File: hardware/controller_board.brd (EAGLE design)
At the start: 86 x 65.5 mm, 249 parts, among them J1 FRSKY-GIMBAL-FRYSKY, J11 USB-MICROA-AMPHENOL-10118192-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, J2 FRSKY-GIMBAL-FRYSKY, J3 USB-MINIB-EDAC-690-005-299-043, J4 AVR_SPI_PRG_6NS, J5 JUMPER-SMT_2_NC_PASTE_NO-SILK, J8 FRSKY-GIMBAL-2X-SERVO, J9 FRSKY-GIMBAL-2X-SERVO, P1 TEST-POINT, P2 TEST-POINT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

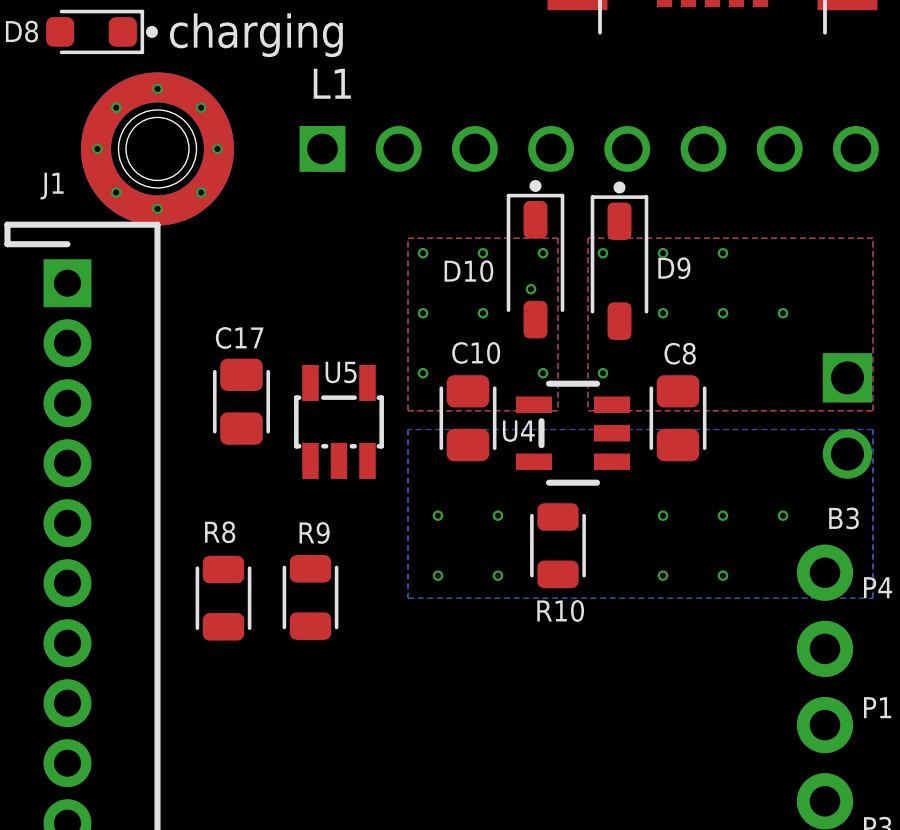
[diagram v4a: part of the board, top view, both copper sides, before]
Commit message: small tweaks to increase symmetry
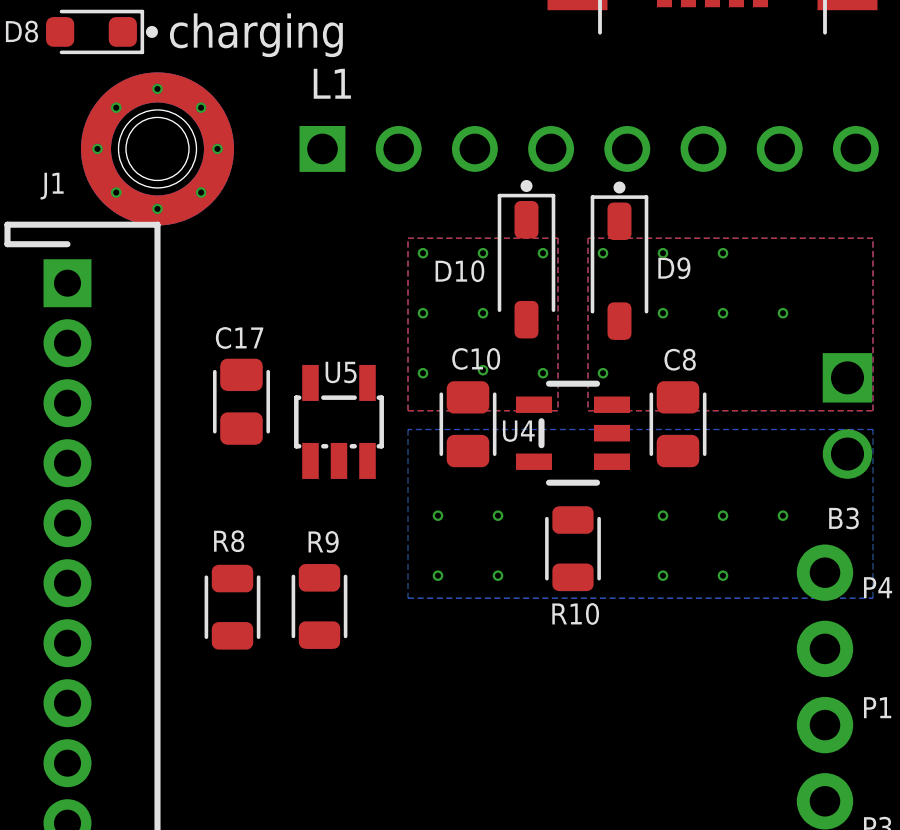
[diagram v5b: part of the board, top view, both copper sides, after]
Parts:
- moved V25 3.14 mm to (-26.6, 10.8)
- moved R10 0.51 mm to (-23.6, 4.80)
- moved R8 0.42 mm to (-35.0, 2.85)
- moved R9 0.42 mm to (-32.1, 2.88)
- moved D10 0.30 mm to (-25.2, 14.1)
- moved C10 0.20 mm to (-27.1, 8.95)
- moved C8 0.20 mm to (-20.1, 8.95)

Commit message: simplify design
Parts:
- R11: value 270 -> 510

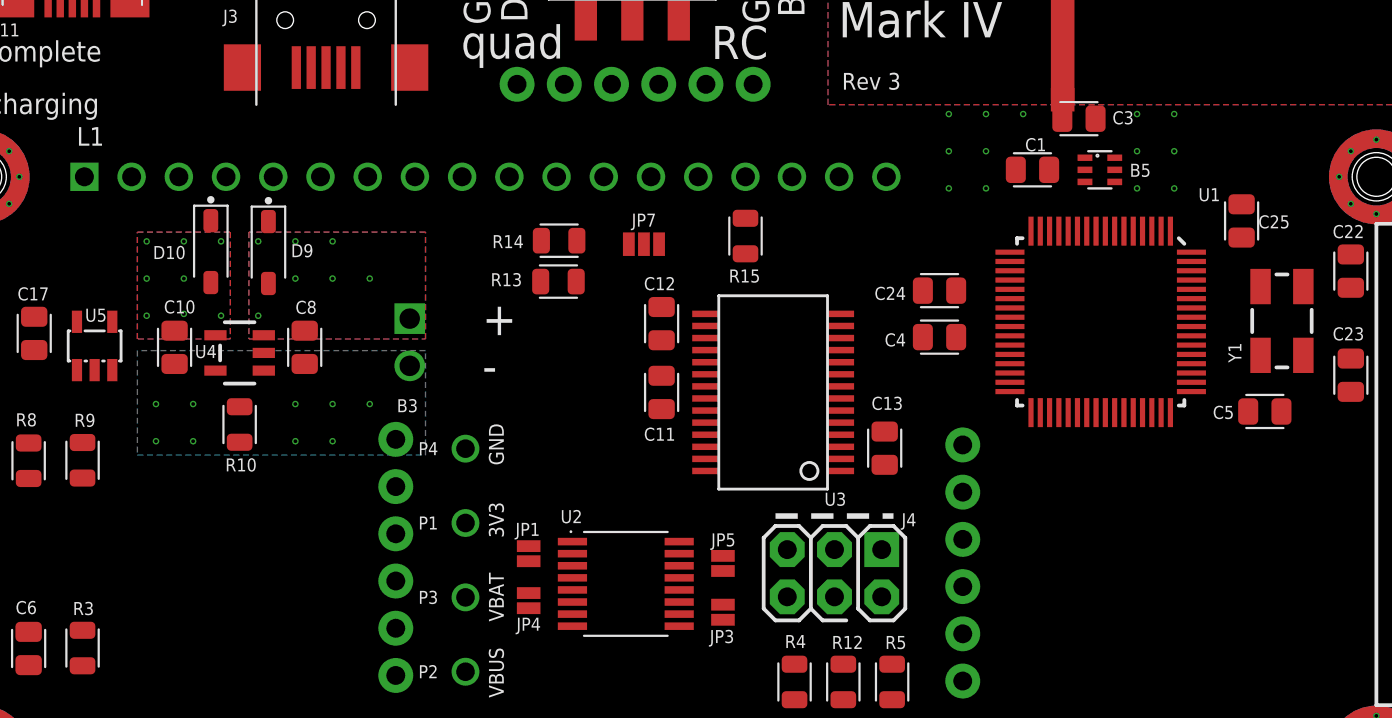
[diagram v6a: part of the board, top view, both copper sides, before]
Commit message: added configuration jumpers for AREF
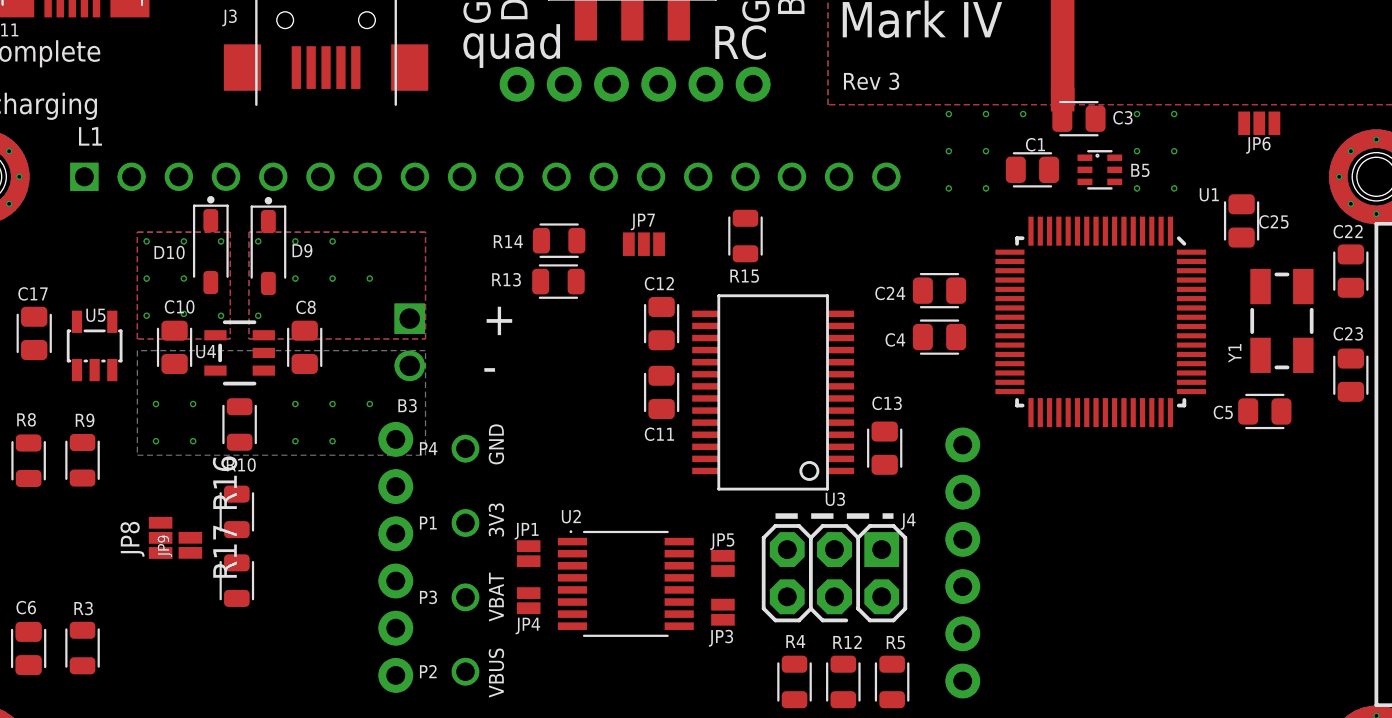
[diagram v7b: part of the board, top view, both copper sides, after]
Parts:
- added JP6, JP8: JUMPER-SMT_3_1-NC_PASTE_NO-SILK, RemoteParts:SMT-JUMPER_3_1-NC_PASTE_NO-SILK
- added JP9: JUMPER-SMT_2_NO_NO-SILK, RemoteParts:SMT-JUMPER_2_NO_NO-SILK
- added R16, R17: 1K, quadparts_prebuilt:RESC2012X60_HS
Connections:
- new net AREF: JP6.2, JP8.1, U1.62
- new net AVDD: JP6.1
- new net GREF: J1.1, J1.4, J2.1, J2.4, J8.1, J8.4, J9.1, J9.4, JP8.2, JP9.2
- new net V3V/2: JP9.1, R16.1, R17.2
- net 3V3: now also JP6.3, JP8.3, R16.2; no longer J1.1, J1.4, J2.1, J2.4, J8.1, J8.4, J9.1, J9.4, U1.62
- net GND: now also R17.1

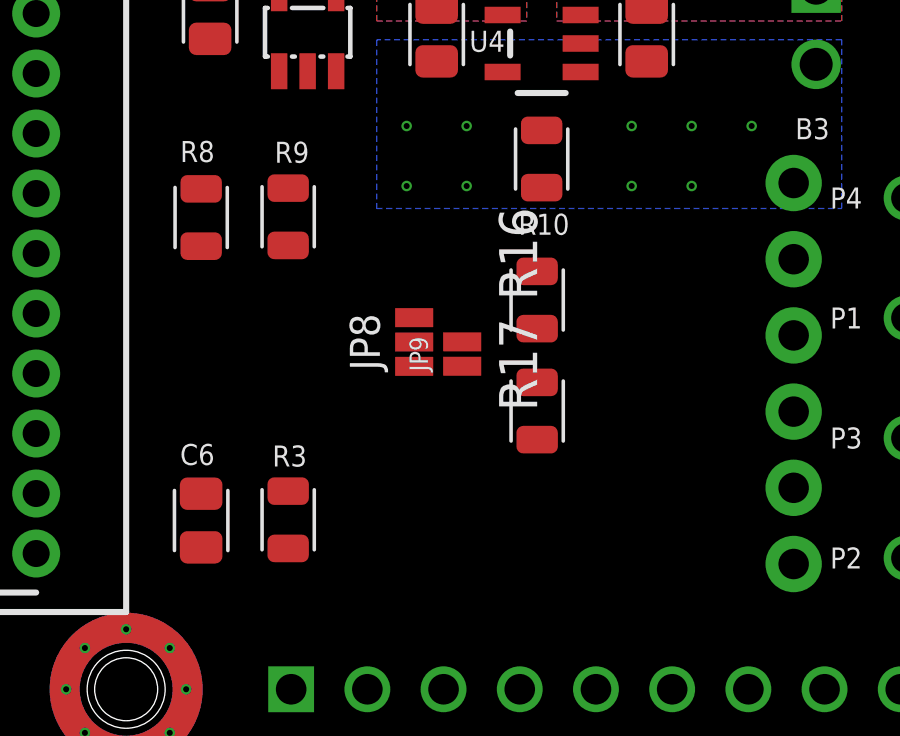
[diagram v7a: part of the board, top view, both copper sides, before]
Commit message: silkscreen touch up
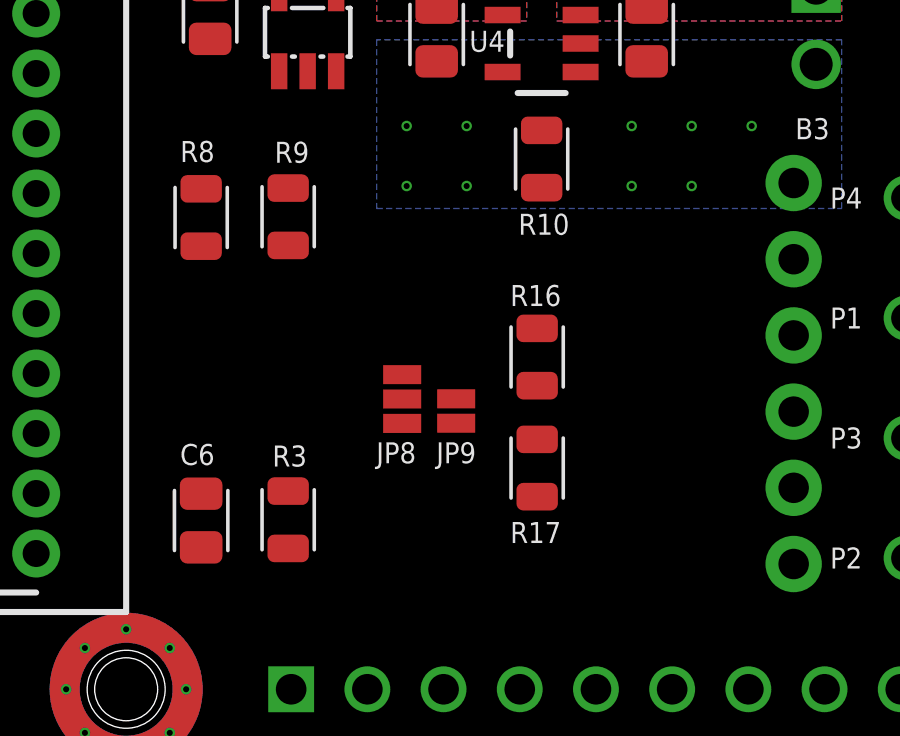
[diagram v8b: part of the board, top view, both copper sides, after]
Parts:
- moved JP8 1.94 mm to (-28.3, -3.20)
- moved JP9 1.91 mm to (-26.5, -3.60)
- moved R16 1.90 mm to (-23.8, -1.80)
- moved R17 1.90 mm to (-23.8, -5.50)
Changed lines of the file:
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@@
 <attribute name="NAME" x="31.2" y="20.257" size="0.7" layer="25" font="vector" rot="R180" align="bottom-center"/>
 </element>
-<element name="JP8" library="RemoteParts" package="SMT-JUMPER_3_1-NC_PASTE_NO-SILK" value="JUMPER-SMT_3_1-NC_PASTE_NO-SILK" x="-27.9" y="-1.3" rot="R90"/>
-<element name="R16" library="quadparts_prebuilt" package="RESC2012X60_HS" value="1K" x="-23.8" y="0.1" rot="R90">
-<attribute name="CREATOR" value="Swanson" x="-23.8" y="0.1" size="1.778" layer="27" rot="R90" display="off"/>
-<attribute name="DIST" value="DIGIKEY" x="-23.8" y="0.1" size="1.778" layer="27" rot="R90" display="off"/>
-<attribute name="DISTPN" value="311-1.0KARCT-ND" x="-23.8" y="0.1" size="1.778" layer="27" rot="R90" display="off"/>
+<element name="JP8" library="RemoteParts" package="SMT-JUMPER_3_1-NC_PASTE_NO-SILK" value="JUMPER-SMT_3_1-NC_PASTE_NO-SILK" x="-28.3" y="-3.2" smashed="yes" rot="R90">
+<attribute name="NAME" x="-28.5" y="-4.643" size="0.7" layer="25" font="vector" rot="R180" align="bottom-center"/>
 </element>
-<element name="R17" library="quadparts_prebuilt" package="RESC2012X60_HS" value="1K" x="-23.8" y="-3.6" rot="R90">
-<attribute name="CREATOR" value="Swanson" x="-23.8" y="-3.6" size="1.778" layer="27" rot="R90" display="off"/>
-<attribute name="DIST" value="DIGIKEY" x="-23.8" y="-3.6" size="1.778" layer="27" rot="R90" display="off"/>
-<attribute name="DISTPN" value="311-1.0KARCT-ND" x="-23.8" y="-3.6" size="1.778" layer="27" rot="R90" display="off"/>
+<element name="R16" library="quadparts_prebuilt" package="RESC2012X60_HS" value="1K" x="-23.8" y="-1.8" smashed="yes" rot="R90">
+<attribute name="CREATOR" value="Swanson" x="-23.8" y="-1.8" size="1.778" layer="27" rot="R90" display="off"/>
+<attribute name="DIST" value="DIGIKEY" x="-23.8" y="-1.8" size="1.778" layer="27" rot="R90" display="off"/>
+<attribute name="DISTPN" value="311-1.0KARCT-ND" x="-23.8" y="-1.8" size="1.778" layer="27" rot="R90" display="off"/>
+<attribute name="NAME" x="-23" y="0.6" size="0.7" layer="25" font="vector" rot="R180"/>
+<attribute name="VALUE" x="-22" y="-2.3" size="0.7" layer="27" font="vector" ratio="10" rot="R90"/>
 </element>
-<element name="JP9" library="RemoteParts" package="SMT-JUMPER_2_NO_NO-SILK" value="JUMPER-SMT_2_NO_NO-SILK" x="-26.3" y="-1.7" rot="R90"/>
+<element name="R17" library="quadparts_prebuilt" package="RESC2012X60_HS" value="1K" x="-23.8" y="-5.5" smashed="yes" rot="R90">
+<attribute name="CREATOR" value="Swanson" x="-23.8" y="-5.5" size="1.778" layer="27" rot="R90" display="off"/>
+<attribute name="DIST" value="DIGIKEY" x="-23.8" y="-5.5" size="1.778" layer="27" rot="R90" display="off"/>
+<attribute name="DISTPN" value="311-1.0KARCT-ND" x="-23.8" y="-5.5" size="1.778" layer="27" rot="R90" display="off"/>
+<attribute name="NAME" x="-23" y="-7.3" size="0.7" layer="25" font="vector" rot="R180"/>
+<attribute name="VALUE" x="-22" y="-6" size="0.7" layer="27" font="vector" ratio="10" rot="R90"/>
+</element>
+<element name="JP9" library="RemoteParts" package="SMT-JUMPER_2_NO_NO-SILK" value="JUMPER-SMT_2_NO_NO-SILK" x="-26.5" y="-3.6" smashed="yes" rot="R90">
+<attribute name="NAME" x="-26.5" y="-4.643" size="0.7" layer="25" font="vector" rot="R180" align="bottom-center"/>
+</element>
 </elements>
 <signals>
@@
 <contactref element="S2" pad="A"/>
 <contactref element="R17" pad="1"/>
-<wire x1="-39.6" y1="-20.5" x2="-23.8" y2="-4.555" width="0" layer="19" extent="1-1"/>
+<wire x1="-39.6" y1="-20.5" x2="-23.8" y2="-6.455" width="0" layer="19" extent="1-1"/>
 <wire x1="-28.45" y1="-23.53" x2="-32.4" y2="-20.5" width="0" layer="19" extent="1-1"/>
 <wire x1="-25.95" y1="-25.62" x2="-28.45" y2="-23.53" width="0" layer="19" extent="1-1"/>
@@
 <contactref element="JP8" pad="3"/>
 <contactref element="R16" pad="2"/>
-<wire x1="-27.9" y1="-0.4872" x2="-23.8" y2="1.055" width="0" layer="19" extent="1-1"/>
-<wire x1="-23.845" y1="-28.675" x2="-27.9" y2="-0.4872" width="0" layer="19" extent="1-1"/>
+<wire x1="-28.3" y1="-2.3872" x2="-23.8" y2="-0.845" width="0" layer="19" extent="1-1"/>
+<wire x1="-23.845" y1="-28.675" x2="-28.3" y2="-2.3872" width="0" layer="19" extent="1-1"/>
 <wire x1="-32.1" y1="-6.27" x2="-23.845" y2="-28.675" width="0" layer="19" extent="1-1"/>
 <wire x1="-32.4" y1="10.325" x2="-32.1" y2="-6.27" width="0" layer="19" extent="1-1"/>
@@
 <contactref element="U1" pad="62"/>
 <contactref element="JP8" pad="1"/>
-<wire x1="27.551" y1="13.07" x2="-27.9" y2="-2.1128" width="0" layer="19" extent="1-1"/>
+<wire x1="27.551" y1="13.07" x2="-28.3" y2="-4.0128" width="0" layer="19" extent="1-1"/>
 <wire x1="31.2" y1="21" x2="27.551" y2="13.07" width="0" layer="19" extent="1-1"/>
 </signal>
@@
 <contactref element="J8" pad="4"/>
 <contactref element="JP9" pad="2"/>
-<wire x1="-27.9" y1="-1.3" x2="-26.3" y2="-1.2936" width="0" layer="19" extent="1-1"/>
-<wire x1="-40.5" y1="7.65" x2="-27.9" y2="-1.3" width="0" layer="19" extent="1-1"/>
+<wire x1="-28.3" y1="-3.2" x2="-26.5" y2="-3.1936" width="0" layer="19" extent="1-1"/>
+<wire x1="-40.5" y1="7.65" x2="-28.3" y2="-3.2" width="0" layer="19" extent="1-1"/>
 <wire x1="-40.5" y1="13.65" x2="-40.5" y2="7.65" width="0" layer="19" extent="1-1"/>
 <wire x1="-15.25" y1="4" x2="-40.5" y2="7.65" width="0" layer="19" extent="1-1"/>
@@
 <contactref element="R17" pad="2"/>
 <contactref element="JP9" pad="1"/>
-<wire x1="-23.8" y1="-2.645" x2="-26.3" y2="-2.1064" width="0" layer="19" extent="1-1"/>
-<wire x1="-23.8" y1="-0.855" x2="-23.8" y2="-2.645" width="0" layer="19" extent="1-1"/>
+<wire x1="-23.8" y1="-4.545" x2="-26.5" y2="-4.0064" width="0" layer="19" extent="1-1"/>
+<wire x1="-23.8" y1="-2.755" x2="-23.8" y2="-4.545" width="0" layer="19" extent="1-1"/>
 </signal>
 </signals>
